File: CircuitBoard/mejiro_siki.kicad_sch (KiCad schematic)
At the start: 58 parts, among them J1 MJ-4PP-9, J2 MJ-4PP-9, SW1 SW_Push, SW10 SW_Push, SW11 SW_Push, SW12 SW_Push, SW13 SW_Push, SW14 SW_Push, SW15 SW_Push, SW16 SW_Push, SW17 SW_Push, SW18 SW_Push, SW19 SW_Push, SW2 SW_Push, SW20 SW_Push, SW21 SW_Push, SW22 SW_Push, SW23 SW_Push, SW24 SW_Push, SW25 SW_Push, SW26 SW_Push, SW3 SW_Push, SW4 SW_Push, SW5 SW_Push, SW6 SW_Push, SW7 SW_Push, SW8 SW_Push, SW9 SW_Push, U1 XIAO-nRF52840-SMD, U2 XIAO-nRF52840-SMD

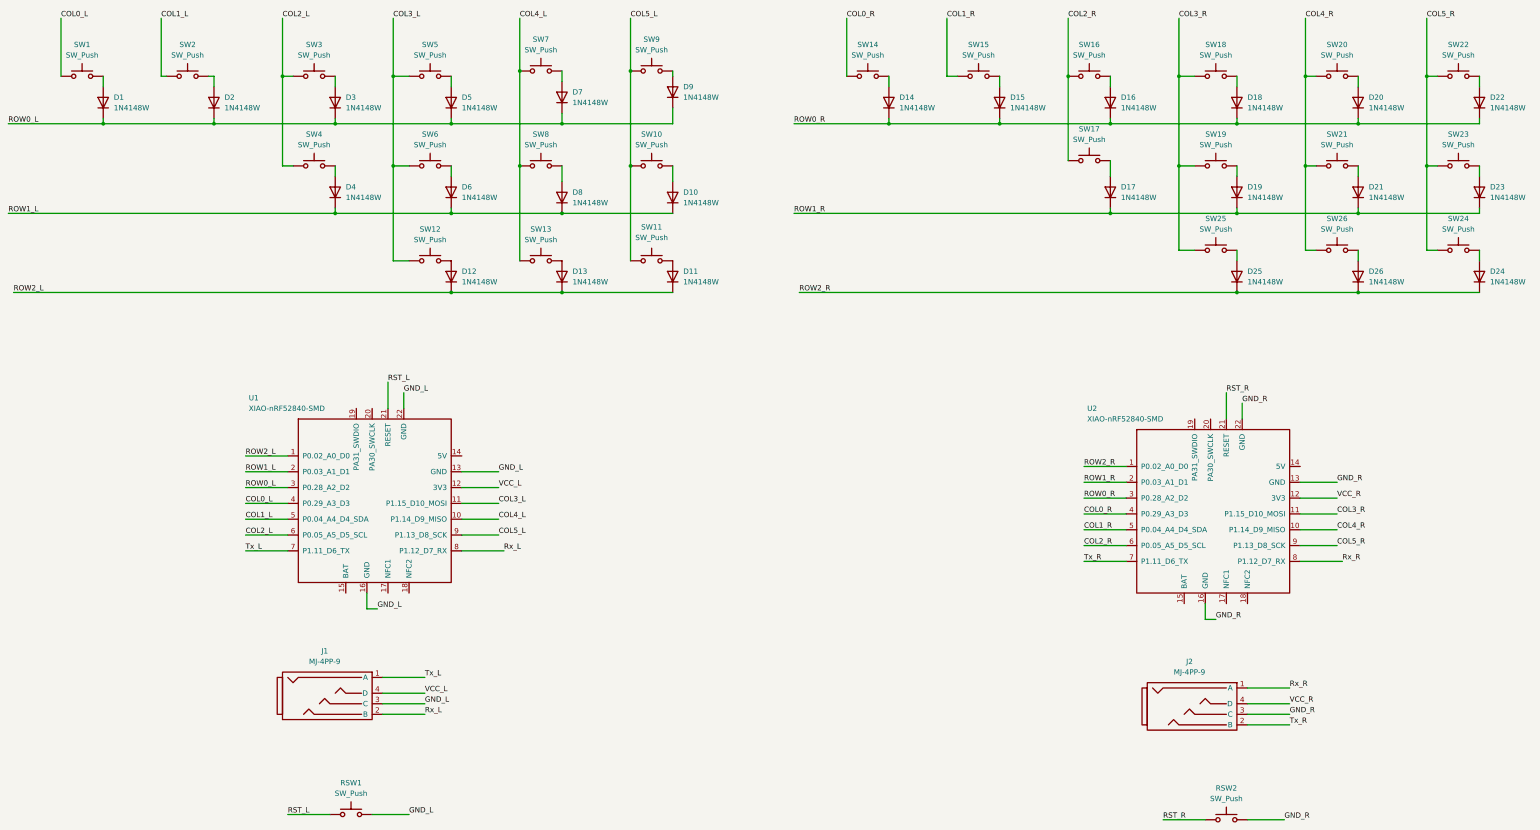
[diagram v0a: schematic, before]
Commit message: 基板更新(laptwing対応)
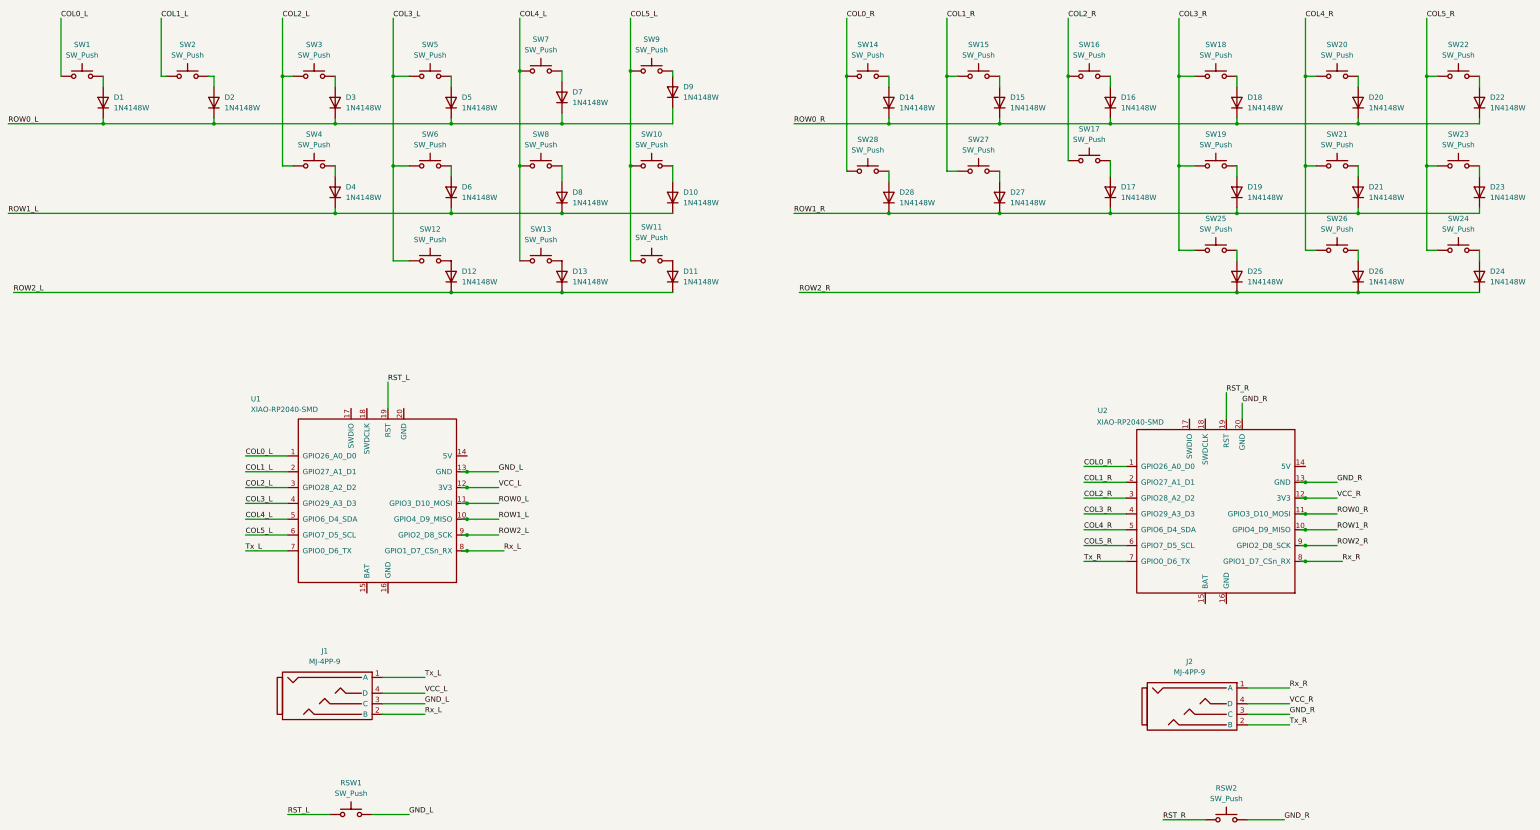
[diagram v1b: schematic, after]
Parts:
- removed U1, U2: XIAO-nRF52840-SMD, mejiro_footprint:XIAO-nRF52840-SMD, symbol Seeed_Studio_XIAO_Series:XIAO-nRF52840-SMD
- added D27, D28: 1N4148W, Diode_SMD:D_SOD-123, symbol Diode:1N4148W
- added SW27, SW28: SW_Push, BrownSugar_KBD:CherryMX_Hotswap_via_1U, symbol Switch:SW_Push
- added U1, U2: XIAO-RP2040-SMD, XIAO_PCB:XIAO-RP2040-SMD, symbol Seeed_Studio_XIAO_Series:XIAO-RP2040-SMD
- RSW1, RSW2: footprint mejiro_footprint:SKHLLCA010 -> myfootprint:SKHLLCA010
- SW1, SW10, SW11, SW12, SW13, SW14, SW15, SW16, SW17, SW18, SW19, SW2, SW20, SW21, SW22, SW23, SW24, SW25, SW26, SW3, SW4, SW5, SW6, SW7, SW8, SW9: footprint keyswitches:Kailh_socket_MX -> BrownSugar_KBD:CherryMX_Hotswap_via_1U
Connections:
- net COL0_L: now also U1.1 (GPIO26_A0_D0)
- net COL0_R: now also SW28.1, U2.1 (GPIO26_A0_D0)
- net COL1_L: now also U1.2 (GPIO27_A1_D1)
- net COL1_R: now also SW27.1, U2.2 (GPIO27_A1_D1)
- net COL2_L: now also U1.3 (GPIO28_A2_D2)
- net COL2_R: now also U2.3 (GPIO28_A2_D2)
- net COL3_L: now also U1.4 (GPIO29_A3_D3)
- net COL3_R: now also U2.4 (GPIO29_A3_D3)
- net COL4_L: now also U1.5 (GPIO6_D4_SDA)
- net COL4_R: now also U2.5 (GPIO6_D4_SDA)
- net COL5_L: now also U1.6 (GPIO7_D5_SCL)
- net COL5_R: now also U2.6 (GPIO7_D5_SCL)
- net GND_L: now also U1.13 (GND)
- net GND_R: now also U2.13 (GND), U2.20 (GND)
- net ROW0_L: now also U1.11 (GPIO3_D10_MOSI)
- net ROW0_R: now also U2.11 (GPIO3_D10_MOSI)
- net ROW1_L: now also U1.10 (GPIO4_D9_MISO)
- net ROW1_R: now also D27.1 (K), D28.1 (K), U2.10 (GPIO4_D9_MISO)
- net ROW2_L: now also U1.9 (GPIO2_D8_SCK)
- net ROW2_R: now also U2.9 (GPIO2_D8_SCK)
- net RST_L: now also U1.19 (RST)
- net RST_R: now also U2.19 (RST)
- net Rx_L: now also U1.8 (GPIO1_D7_CSn_RX)
- net Rx_R: now also U2.8 (GPIO1_D7_CSn_RX)
- net Tx_L: now also U1.7 (GPIO0_D6_TX)
- net Tx_R: now also U2.7 (GPIO0_D6_TX)
- net VCC_L: now also U1.12 (3V3)
- net VCC_R: now also U2.12 (3V3)
- new net: D27.2 (A), SW27.2
- new net: D28.2 (A), SW28.2
